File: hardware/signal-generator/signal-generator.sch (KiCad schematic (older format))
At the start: 40 parts, among them J1 AVR-ISP-6, J10 Output_Conn, J2 AVR_SPI, J3 PORT_G, J4 PORT_F, J5 PORT_E, J6 PORT_A, J7 PORT_C, J8 AREF, J9 Power_Supply_Rails, SW1 RESET_BUTTON, U1 74HC04, U2 74HC08, U3 74HC08, U4 74HC30, U5 ATmega2561-16AU, U6 ADP7142AUJZ-5.0, U7 TC1017-3.3VCTTR, Y1 16MHz

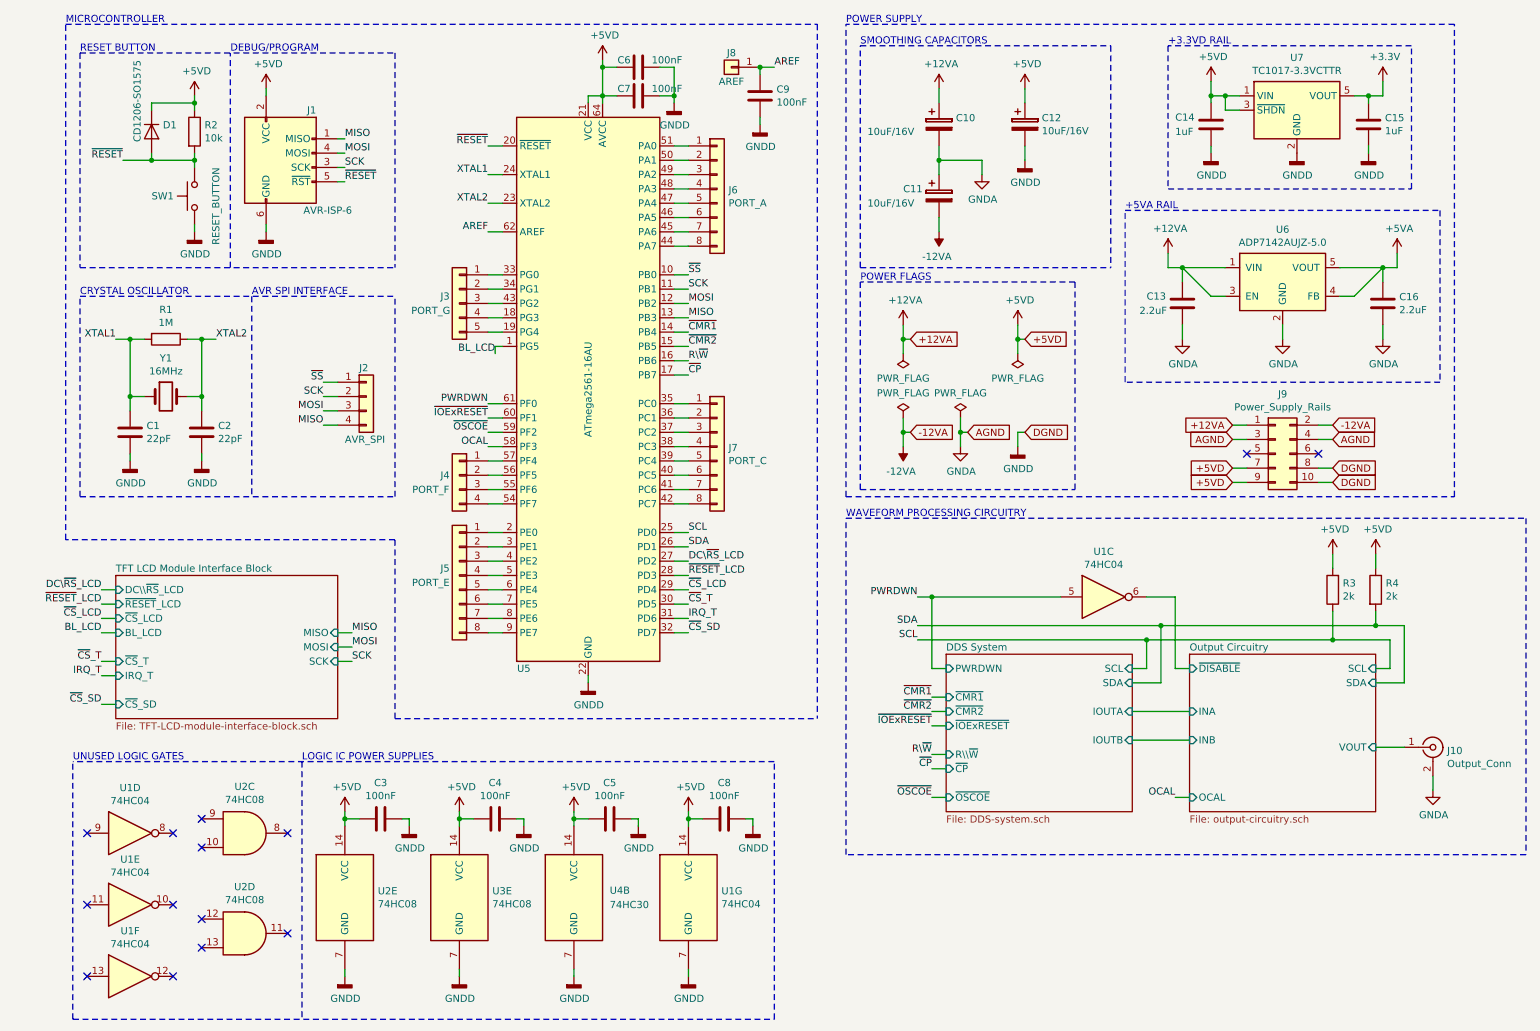
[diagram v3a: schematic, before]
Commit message: [Signal Generator] Complete DDS system layout and routing
All components of the DDS system, as well as their supporting parts, are
laid out compactly on the board.
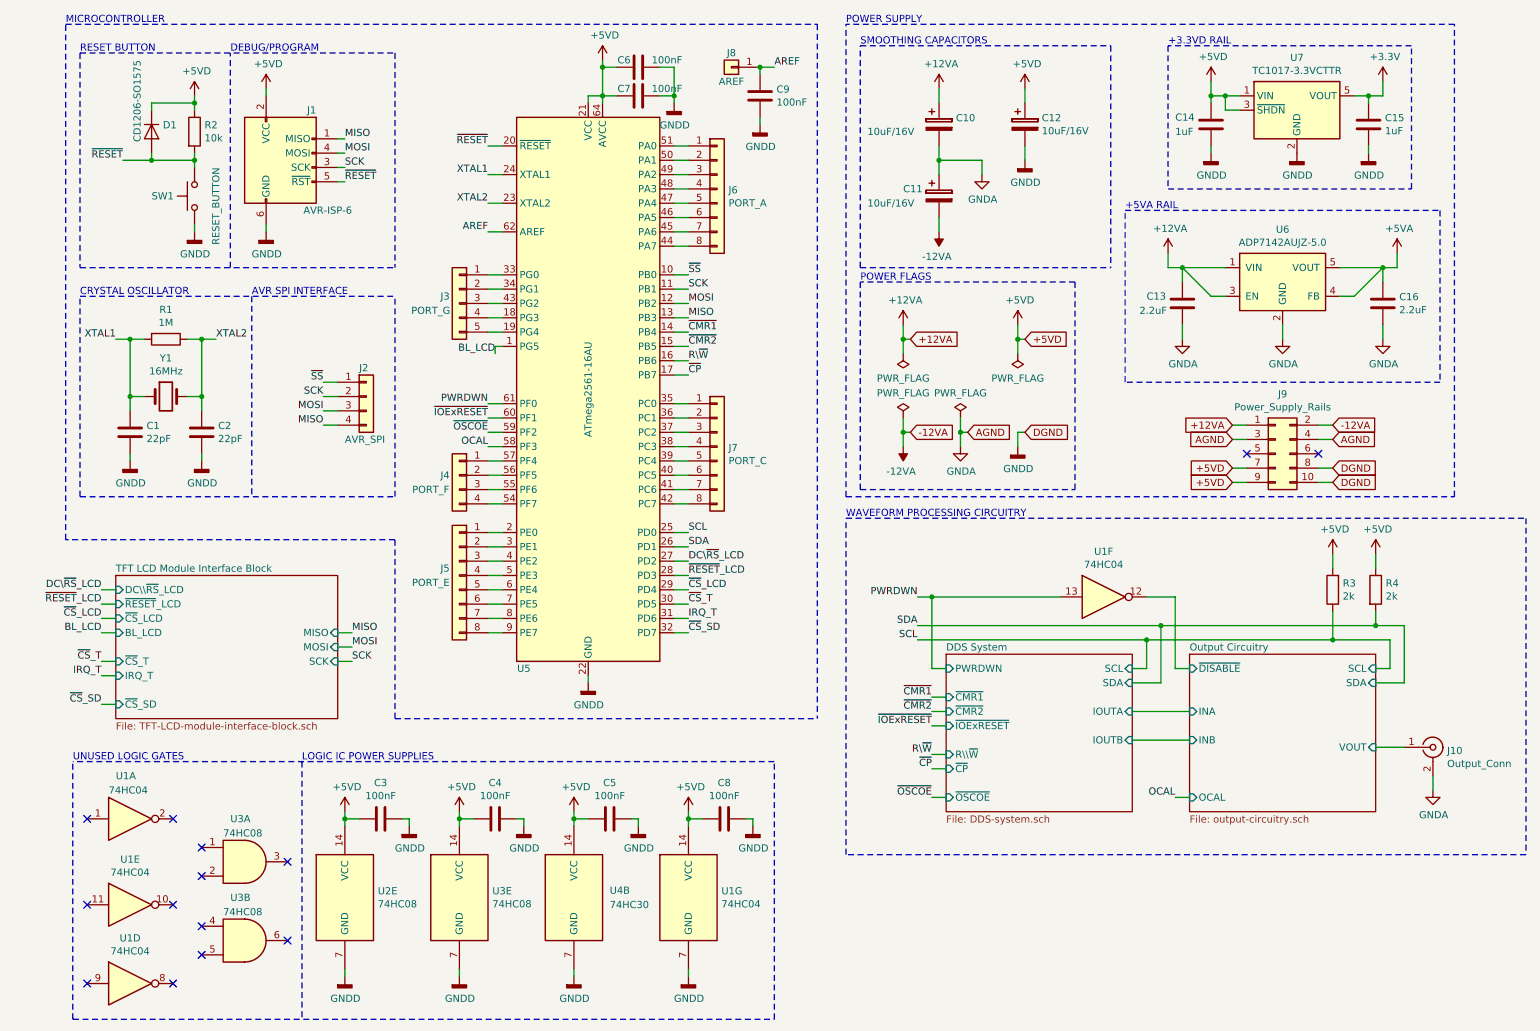
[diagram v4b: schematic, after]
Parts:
- removed unit 3 of U1
- removed unit 3 of U2
- removed unit 4 of U2
- added unit 1 of U1
- added unit 1 of U3
- added unit 2 of U3
- U1: footprint Housings_SOIC:SOIC-14_3.9x8.7mm_Pitch1.27mm -> (none)
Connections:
- net Output Circuitry/~DISABLE: now also U1.12
- net PWRDWN: now also U1.13
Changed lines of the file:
@@
 Sheet 1 5
 Title "Digital Function Generator v2"
-Date "2019-12-21"
+Date "2019-12-26"
 Rev "1"
 Comp "Petar Nikolov"
@@
 Wire Wire Line
 	8650 5100 8550 5100
-$Comp
-L 74xx:74HC04 U1
-U 3 1 5E03ECE0
-P 8050 4600
-F 0 "U1" H 8050 4917 50  0000 C CNN
-F 1 "74HC04" H 8050 4826 50  0000 C CNN
-F 2 "Housings_SOIC:SOIC-14_3.9x8.7mm_Pitch1.27mm" H 8050 4600 50  0001 C CNN
-F 3 "https://assets.nexperia.com/documents/data-sheet/74HC_HCT04.pdf" H 8050 4600 50  0001 C CNN
-	3    8050 4600
-	1    0    0    -1
-$EndComp
 Wire Wire Line
 	8350 4600 8550 4600
@@
 Text Notes 6250 4050 0    50   ~ 0
 WAVEFORM PROCESSING CIRCUITRY
-NoConn ~ 1750 6150
-NoConn ~ 1750 6350
-NoConn ~ 1750 6850
-NoConn ~ 1750 7050
-NoConn ~ 2350 6950
-NoConn ~ 2350 6250
 $Comp
 L Device:C C?
@@
 $EndComp
 $Comp
-L ulib_MY_74xx:74HC08 U?
-U 3 1 5DE93472
-P 2050 6250
-AR Path="/5DB72CF6/5DBBB708/5DE93472" Ref="U?"  Part="3"
-AR Path="/5DE65B3D/5DE93472" Ref="U?"  Part="3"
-AR Path="/5DE93472" Ref="U2"  Part="3"
-F 0 "U2" H 2050 6575 50  0000 C CNN
-F 1 "74HC08" H 2050 6484 50  0000 C CNN
-F 2 "Housings_SOIC:SOIC-14_3.9x8.7mm_Pitch1.27mm" H 2050 6200 50  0001 C CNN
-F 3 "https://assets.nexperia.com/documents/data-sheet/74HC_HCT08.pdf" H 2050 6300 50  0001 C CNN
-	3    2050 6250
-	1    0    0    -1
-$EndComp
-$Comp
-L ulib_MY_74xx:74HC08 U?
-U 4 1 5DE93479
-P 2050 6950
-AR Path="/5DB72CF6/5DBBB708/5DE93479" Ref="U?"  Part="4"
-AR Path="/5DE65B3D/5DE93479" Ref="U?"  Part="4"
-AR Path="/5DE93479" Ref="U2"  Part="4"
-F 0 "U2" H 2050 7275 50  0000 C CNN
-F 1 "74HC08" H 2050 7184 50  0000 C CNN
-F 2 "Housings_SOIC:SOIC-14_3.9x8.7mm_Pitch1.27mm" H 2050 6900 50  0001 C CNN
-F 3 "https://assets.nexperia.com/documents/data-sheet/74HC_HCT08.pdf" H 2050 7000 50  0001 C CNN
-	4    2050 6950
-	1    0    0    -1
-$EndComp
-$Comp
-L 74xx:74HC04 U1
-U 4 1 5DE93480
-P 1250 6250
-F 0 "U1" H 1250 6567 50  0000 C CNN
-F 1 "74HC04" H 1250 6476 50  0000 C CNN
-F 2 "Housings_SOIC:SOIC-14_3.9x8.7mm_Pitch1.27mm" H 1250 6250 50  0001 C CNN
-F 3 "https://assets.nexperia.com/documents/data-sheet/74HC_HCT04.pdf" H 1250 6250 50  0001 C CNN
-	4    1250 6250
-	1    0    0    -1
-$EndComp
-$Comp
 L 74xx:74HC04 U1
 U 5 1 5DE93487
@@
 F 3 "https://assets.nexperia.com/documents/data-sheet/74HC_HCT04.pdf" H 1250 6750 50  0001 C CNN
 	5    1250 6750
-	1    0    0    -1
-$EndComp
-$Comp
-L 74xx:74HC04 U1
-U 6 1 5DE9348E
-P 1250 7250
-F 0 "U1" H 1250 7567 50  0000 C CNN
-F 1 "74HC04" H 1250 7476 50  0000 C CNN
-F 2 "Housings_SOIC:SOIC-14_3.9x8.7mm_Pitch1.27mm" H 1250 7250 50  0001 C CNN
-F 3 "https://assets.nexperia.com/documents/data-sheet/74HC_HCT04.pdf" H 1250 7250 50  0001 C CNN
-	6    1250 7250
 	1    0    0    -1
 $EndComp
@@
 	1    0    0    -1
 $EndComp
-NoConn ~ 1550 7250
 NoConn ~ 1550 6750
-NoConn ~ 1550 6250
-NoConn ~ 950  6250
 NoConn ~ 950  6750
-NoConn ~ 950  7250
 Wire Notes Line
 	850  7550 850  5750
@@
 Text Label 8550 6000 2    50   ~ 0
 OCAL
+$Comp
+L ulib_MY_74xx:74HC08 U?
+U 1 1 5E18D9E0
+P 2050 6450
+AR Path="/5DB72CF6/5DBBB708/5E18D9E0" Ref="U?"  Part="1"
+AR Path="/5E18D9E0" Ref="U3"  Part="1"
+F 0 "U3" H 1950 6750 50  0000 L CNN
+F 1 "74HC08" H 1900 6650 50  0000 L CNN
+F 2 "Housings_SOIC:SOIC-14_3.9x8.7mm_Pitch1.27mm" H 2050 6400 50  0001 C CNN
+F 3 "https://assets.nexperia.com/documents/data-sheet/74HC_HCT08.pdf" H 2050 6500 50  0001 C CNN
+	1    2050 6450
+	1    0    0    -1
+$EndComp
+$Comp
+L ulib_MY_74xx:74HC08 U?
+U 2 1 5E18D9E6
+P 2050 7000
+AR Path="/5DB72CF6/5DBBB708/5E18D9E6" Ref="U?"  Part="2"
+AR Path="/5E18D9E6" Ref="U3"  Part="2"
+F 0 "U3" H 1950 7300 50  0000 L CNN
+F 1 "74HC08" H 1900 7200 50  0000 L CNN
+F 2 "Housings_SOIC:SOIC-14_3.9x8.7mm_Pitch1.27mm" H 2050 6950 50  0001 C CNN
+F 3 "https://assets.nexperia.com/documents/data-sheet/74HC_HCT08.pdf" H 2050 7050 50  0001 C CNN
+	2    2050 7000
+	1    0    0    -1
+$EndComp
+NoConn ~ 1750 6350
+NoConn ~ 1750 6550
+NoConn ~ 1750 6900
+NoConn ~ 1750 7100
+NoConn ~ 2350 7000
+NoConn ~ 2350 6450
+$Comp
+L 74xx:74HC04 U?
+U 1 1 5E394027
+P 1250 6150
+AR Path="/5DB72CF6/5DBBB708/5E394027" Ref="U?"  Part="1"
+AR Path="/5E394027" Ref="U1"  Part="1"
+F 0 "U1" H 1150 6450 50  0000 L CNN
+F 1 "74HC04" H 1100 6350 50  0000 L CNN
+F 2 "Housings_SOIC:SOIC-14_3.9x8.7mm_Pitch1.27mm" H 1250 6150 50  0001 C CNN
+F 3 "https://assets.nexperia.com/documents/data-sheet/74HC_HCT04.pdf" H 1250 6150 50  0001 C CNN
+	1    1250 6150
+	1    0    0    -1
+$EndComp
+NoConn ~ 1550 6150
+NoConn ~ 950  6150
+$Comp
+L 74xx:74HC04 U1
+U 4 1 5E3FD50C
+P 1250 7300
+AR Path="/5E3FD50C" Ref="U1"  Part="4"
+AR Path="/5DB72CF6/5DBBB708/5E3FD50C" Ref="U?"  Part="4"
+F 0 "U1" H 1250 7617 50  0000 C CNN
+F 1 "74HC04" H 1250 7526 50  0000 C CNN
+F 2 "Housings_SOIC:SOIC-14_3.9x8.7mm_Pitch1.27mm" H 1250 7300 50  0001 C CNN
+F 3 "https://assets.nexperia.com/documents/data-sheet/74HC_HCT04.pdf" H 1250 7300 50  0001 C CNN
+	4    1250 7300
+	1    0    0    -1
+$EndComp
+NoConn ~ 950  7300
+NoConn ~ 1550 7300
+$Comp
+L 74xx:74HC04 U1
+U 6 1 5E460C5F
+P 8050 4600
+F 0 "U1" H 8050 4917 50  0000 C CNN
+F 1 "74HC04" H 8050 4826 50  0000 C CNN
+F 2 "" H 8050 4600 50  0001 C CNN
+F 3 "https://assets.nexperia.com/documents/data-sheet/74HC_HCT04.pdf" H 8050 4600 50  0001 C CNN
+	6    8050 4600
+	1    0    0    -1
+$EndComp
 $EndSCHEMATC

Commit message: [Signal Generator] Rework DDS system PCB layout
The previous layout of the DDS system had its components rather
awkwardly positioned. Furthermore, it did not take into account the
distinction of the digital and analog grounds, as well as their star
ground connection.
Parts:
- removed unit 1 of U1
- added unit 3 of U1
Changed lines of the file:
@@
 Sheet 1 5
 Title "Digital Function Generator v2"
-Date "2019-12-26"
+Date "2019-12-28"
 Rev "1"
 Comp "Petar Nikolov"
@@
 NoConn ~ 2350 6450
 $Comp
-L 74xx:74HC04 U?
-U 1 1 5E394027
-P 1250 6150
-AR Path="/5DB72CF6/5DBBB708/5E394027" Ref="U?"  Part="1"
-AR Path="/5E394027" Ref="U1"  Part="1"
-F 0 "U1" H 1150 6450 50  0000 L CNN
-F 1 "74HC04" H 1100 6350 50  0000 L CNN
-F 2 "Housings_SOIC:SOIC-14_3.9x8.7mm_Pitch1.27mm" H 1250 6150 50  0001 C CNN
-F 3 "https://assets.nexperia.com/documents/data-sheet/74HC_HCT04.pdf" H 1250 6150 50  0001 C CNN
-	1    1250 6150
-	1    0    0    -1
-$EndComp
-NoConn ~ 1550 6150
-NoConn ~ 950  6150
-$Comp
 L 74xx:74HC04 U1
 U 4 1 5E3FD50C
@@
 	1    0    0    -1
 $EndComp
+$Comp
+L 74xx:74HC04 U1
+U 3 1 5E0D16A8
+P 1250 6150
+AR Path="/5E0D16A8" Ref="U1"  Part="3"
+AR Path="/5DB72CF6/5DBBB708/5E0D16A8" Ref="U?"  Part="3"
+F 0 "U1" H 1250 6450 50  0000 C CNN
+F 1 "74HC04" H 1250 6350 50  0000 C CNN
+F 2 "Housings_SOIC:SOIC-14_3.9x8.7mm_Pitch1.27mm" H 1250 6150 50  0001 C CNN
+F 3 "https://assets.nexperia.com/documents/data-sheet/74HC_HCT04.pdf" H 1250 6150 50  0001 C CNN
+	3    1250 6150
+	1    0    0    -1
+$EndComp
+NoConn ~ 1550 6150
+NoConn ~ 950  6150
 $EndSCHEMATC

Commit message: [Signal Generator] Restore PCB layout with new symbol annotations
The new components have been loaded in the PCB file.
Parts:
- U1: footprint (none) -> Housings_SOIC:SOIC-14_3.9x8.7mm_Pitch1.27mm
- renumbered U3 to U2
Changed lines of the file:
@@
 P 2050 6450
 AR Path="/5DB72CF6/5DBBB708/5E18D9E0" Ref="U?"  Part="1"
-AR Path="/5E18D9E0" Ref="U3"  Part="1"
-F 0 "U3" H 1950 6750 50  0000 L CNN
+AR Path="/5E18D9E0" Ref="U2"  Part="1"
+F 0 "U2" H 1950 6750 50  0000 L CNN
 F 1 "74HC08" H 1900 6650 50  0000 L CNN
 F 2 "Housings_SOIC:SOIC-14_3.9x8.7mm_Pitch1.27mm" H 2050 6400 50  0001 C CNN
@@
 P 2050 7000
 AR Path="/5DB72CF6/5DBBB708/5E18D9E6" Ref="U?"  Part="2"
-AR Path="/5E18D9E6" Ref="U3"  Part="2"
-F 0 "U3" H 1950 7300 50  0000 L CNN
+AR Path="/5E18D9E6" Ref="U2"  Part="2"
+F 0 "U2" H 1950 7300 50  0000 L CNN
 F 1 "74HC08" H 1900 7200 50  0000 L CNN
 F 2 "Housings_SOIC:SOIC-14_3.9x8.7mm_Pitch1.27mm" H 2050 6950 50  0001 C CNN
@@
 F 0 "U1" H 8050 4917 50  0000 C CNN
 F 1 "74HC04" H 8050 4826 50  0000 C CNN
-F 2 "" H 8050 4600 50  0001 C CNN
+F 2 "Housings_SOIC:SOIC-14_3.9x8.7mm_Pitch1.27mm" H 8050 4600 50  0001 C CNN
 F 3 "https://assets.nexperia.com/documents/data-sheet/74HC_HCT04.pdf" H 8050 4600 50  0001 C CNN
 	6    8050 4600

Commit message: [Signal Generator] Layout microcontroller and its peripheral components
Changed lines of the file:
@@
 Sheet 1 5
 Title "Digital Function Generator v2"
-Date "2019-12-28"
+Date "2020-01-02"
 Rev "1"
 Comp "Petar Nikolov"
@@
 U 1 1 5E0935FA
 P 5350 1750
-F 0 "J6" H 5430 1742 50  0000 L CNN
-F 1 "PORT_A" H 5430 1651 50  0000 L CNN
+F 0 "J6" H 5450 1750 50  0000 L CNN
+F 1 "PORT_A" H 5450 1650 50  0000 L CNN
 F 2 "Pin_Headers:Pin_Header_Straight_1x08_Pitch2.54mm" H 5350 1750 50  0001 C CNN
 F 3 "~" H 5350 1750 50  0001 C CNN

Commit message: [Signal Generator] Add an additional bypass capacitor to MCU
The ATMega2561's package has additional power supply pins (for +VCC and
GND). They are hidden in the schematic symbol in KiCad. Nevertheless,
an additional bypass capacitor which is annotated as 'C47' has been
included in the schematic and PCB.
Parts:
- added C47: 100nF, Capacitors_SMD:C_0805_HandSoldering, symbol Device:C
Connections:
- net +5VD: now also C47.1
- net GNDD: now also C47.2
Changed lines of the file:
@@
 Sheet 1 5
 Title "Digital Function Generator v2"
-Date "2020-01-02"
+Date "2020-01-03"
 Rev "1"
 Comp "Petar Nikolov"
@@
 	1    0    0    -1
 $EndComp
-$Comp
-L Device:C C7
-U 1 1 5DD55FF9
-P 4800 1100
-F 0 "C7" V 4750 1000 50  0000 C CNN
-F 1 "100nF" V 4750 1300 50  0000 C CNN
-F 2 "Capacitors_SMD:C_0805_HandSoldering" H 4838 950 50  0001 C CNN
-F 3 "~" H 4800 1100 50  0001 C CNN
-	1    4800 1100
-	0    1    1    0
-$EndComp
-$Comp
-L Device:C C6
-U 1 1 5DD570C2
-P 4800 900
-F 0 "C6" V 4750 800 50  0000 C CNN
-F 1 "100nF" V 4750 1100 50  0000 C CNN
-F 2 "Capacitors_SMD:C_0805_HandSoldering" H 4838 750 50  0001 C CNN
-F 3 "~" H 4800 900 50  0001 C CNN
-	1    4800 900
-	0    1    1    0
-$EndComp
 Wire Wire Line
 	4550 1150 4550 1100
@@
 Wire Wire Line
 	4550 900  4550 1100
-Wire Wire Line
-	4550 900  4550 850
 Connection ~ 4550 900
-$Comp
-L power:+5VD #PWR016
-U 1 1 5DD5BF12
-P 4550 850
-F 0 "#PWR016" H 4550 700 50  0001 C CNN
-F 1 "+5VD" H 4565 1023 50  0000 C CNN
-F 2 "" H 4550 850 50  0001 C CNN
-F 3 "" H 4550 850 50  0001 C CNN
-	1    4550 850
-	1    0    0    -1
-$EndComp
 Wire Wire Line
 	4950 900  5050 900
@@
 NoConn ~ 1550 6150
 NoConn ~ 950  6150
+$Comp
+L Device:C C7
+U 1 1 5DD55FF9
+P 4800 1100
+F 0 "C7" V 4750 1000 50  0000 C CNN
+F 1 "100nF" V 4750 1300 50  0000 C CNN
+F 2 "Capacitors_SMD:C_0805_HandSoldering" H 4838 950 50  0001 C CNN
+F 3 "~" H 4800 1100 50  0001 C CNN
+	1    4800 1100
+	0    1    1    0
+$EndComp
+$Comp
+L Device:C C6
+U 1 1 5DD570C2
+P 4800 900
+F 0 "C6" V 4750 800 50  0000 C CNN
+F 1 "100nF" V 4750 1100 50  0000 C CNN
+F 2 "Capacitors_SMD:C_0805_HandSoldering" H 4838 750 50  0001 C CNN
+F 3 "~" H 4800 900 50  0001 C CNN
+	1    4800 900
+	0    1    1    0
+$EndComp
+Wire Wire Line
+	4550 900  4550 850
+$Comp
+L power:+5VD #PWR016
+U 1 1 5DD5BF12
+P 4550 850
+F 0 "#PWR016" H 4550 700 50  0001 C CNN
+F 1 "+5VD" H 4565 1023 50  0000 C CNN
+F 2 "" H 4550 850 50  0001 C CNN
+F 3 "" H 4550 850 50  0001 C CNN
+	1    4550 850
+	1    0    0    -1
+$EndComp
+Wire Wire Line
+	4450 900  4550 900
+Wire Wire Line
+	4150 900  4050 900
+Wire Wire Line
+	4050 900  4050 1000
+$Comp
+L power:GNDD #PWR0152
+U 1 1 5E1B9C94
+P 4050 1000
+F 0 "#PWR0152" H 4050 750 50  0001 C CNN
+F 1 "GNDD" H 4054 845 50  0000 C CNN
+F 2 "" H 4050 1000 50  0001 C CNN
+F 3 "" H 4050 1000 50  0001 C CNN
+	1    4050 1000
+	1    0    0    -1
+$EndComp
+$Comp
+L Device:C C47
+U 1 1 5E1EEB27
+P 4300 900
+F 0 "C47" V 4150 900 50  0000 C CNN
+F 1 "100nF" V 4450 900 50  0000 C CNN
+F 2 "Capacitors_SMD:C_0805_HandSoldering" H 4338 750 50  0001 C CNN
+F 3 "~" H 4300 900 50  0001 C CNN
+	1    4300 900
+	0    1    1    0
+$EndComp
 $EndSCHEMATC
